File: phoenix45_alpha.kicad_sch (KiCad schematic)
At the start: 140 parts, among them J1 AVR-ISP-6, SW1 SW_PUSH, SW2 SW_PUSH, SW3 RotaryEncoder_Switch, U1 SRV05-4, U2 ATmega32U4-M, U3 ATmega32U4-M, X1 Crystal_GND24_Small

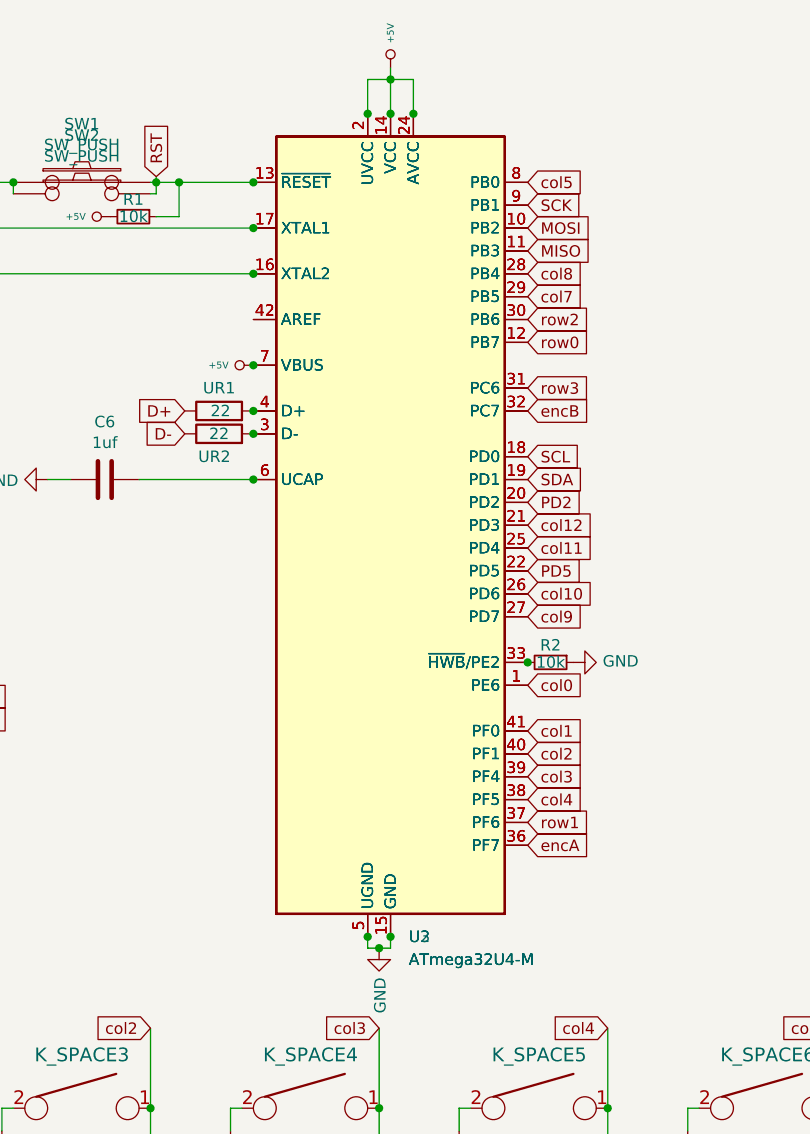
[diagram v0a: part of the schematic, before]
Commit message: atmega32u4-MU only
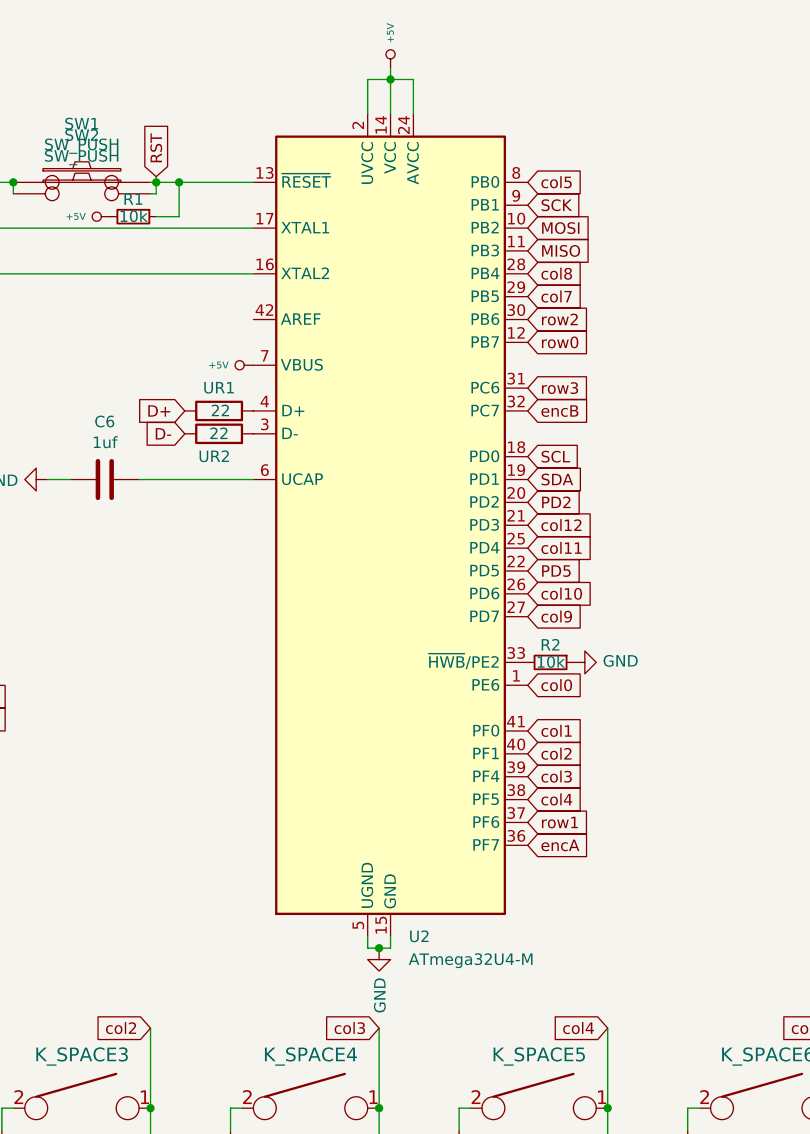
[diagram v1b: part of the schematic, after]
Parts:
- removed U3: ATmega32U4-M, Package_QFP:TQFP-44_10x10mm_P0.8mm, symbol MCU_Microchip_ATmega:ATmega32U4-M
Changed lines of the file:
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@@
   (junction (at 149.86 245.11) (diameter 0) (color 0 0 0 0)
   )
-  (junction (at 127 60.96) (diameter 0) (color 0 0 0 0)
-  )
   (junction (at 166.37 184.15) (diameter 0) (color 0 0 0 0)
   )
   (junction (at 233.045 66.675) (diameter 0) (color 0 0 0 0)
   )
-  (junction (at 142.24 48.26) (diameter 0) (color 0 0 0 0)
-  )
   (junction (at 140.97 158.75) (diameter 0) (color 0 0 0 0)
   )
@@
   (junction (at 140.97 140.97) (diameter 0) (color 0 0 0 0)
   )
-  (junction (at 139.7 139.7) (diameter 0) (color 0 0 0 0)
-  )
   (junction (at 251.46 219.71) (diameter 0) (color 0 0 0 0)
   )
   (junction (at 294.64 109.22) (diameter 0) (color 0 0 0 0)
   )
-  (junction (at 127 66.04) (diameter 0) (color 0 0 0 0)
-  )
   (junction (at 175.26 194.31) (diameter 0) (color 0 0 0 0)
   )
@@
   (junction (at 38.735 105.41) (diameter 0) (color 0 0 0 0)
   )
-  (junction (at 127 88.9) (diameter 0) (color 0 0 0 0)
-  )
   (junction (at 31.115 105.41) (diameter 0) (color 0 0 0 0)
   )
@@
   (junction (at 302.26 219.71) (diameter 0) (color 0 0 0 0)
   )
-  (junction (at 127 55.88) (diameter 0) (color 0 0 0 0)
-  )
   (junction (at 48.26 194.31) (diameter 0) (color 0 0 0 0)
   )
@@
   (junction (at 99.06 231.14) (diameter 0) (color 0 0 0 0)
   )
-  (junction (at 127 76.2) (diameter 0) (color 0 0 0 0)
-  )
   (junction (at 318.77 209.55) (diameter 0) (color 0 0 0 0)
   )
@@
   (junction (at 73.66 194.31) (diameter 0) (color 0 0 0 0)
   )
-  (junction (at 142.24 139.7) (diameter 0) (color 0 0 0 0)
-  )
   (junction (at 251.46 194.31) (diameter 0) (color 0 0 0 0)
   )
   (junction (at 318.77 158.75) (diameter 0) (color 0 0 0 0)
   )
-  (junction (at 139.7 48.26) (diameter 0) (color 0 0 0 0)
-  )
-  (junction (at 127 83.82) (diameter 0) (color 0 0 0 0)
-  )
   (junction (at 293.37 158.75) (diameter 0) (color 0 0 0 0)
   )
@@
   (junction (at 115.57 184.15) (diameter 0) (color 0 0 0 0)
   )
-  (junction (at 144.78 48.26) (diameter 0) (color 0 0 0 0)
-  )
   (junction (at 293.37 229.87) (diameter 0) (color 0 0 0 0)
   )
@@
   (junction (at 267.97 158.75) (diameter 0) (color 0 0 0 0)
   )
-  (junction (at 127 81.28) (diameter 0) (color 0 0 0 0)
-  )
   (junction (at 72.39 77.47) (diameter 0) (color 0 0 0 0)
   )
@@
   (junction (at 344.17 158.75) (diameter 0) (color 0 0 0 0)
   )
-  (junction (at 157.48 109.22) (diameter 0) (color 0 0 0 0)
-  )
   (junction (at 166.37 209.55) (diameter 0) (color 0 0 0 0)
   )
@@
     (pin "2")
   )
-  (symbol (lib_id "MCU_Microchip_ATmega:ATmega32U4-M") (at 142.24 93.98 0) (unit 1)
-    (in_bom yes) (on_board yes)
-    (property "Reference" "U3" (id 0) (at 144.2594 139.7 0)
-      (effects (font (size 1.27 1.27)) (justify left))
-    )
-    (property "Value" "ATmega32U4-M" (id 1) (at 144.2594 142.24 0)
-      (effects (font (size 1.27 1.27)) (justify left))
-    )
-    (property "Footprint" "Package_QFP:TQFP-44_10x10mm_P0.8mm" (id 2) (at 142.24 93.98 0)
-      (effects (font (size 1.27 1.27) italic) hide)
-    )
-    (property "Datasheet" "http://ww1.microchip.com/downloads/en/DeviceDoc/Atmel-7766-8-bit-AVR-ATmega16U4-32U4_Datasheet.pdf" (id 3) (at 142.24 93.98 0)
-      (effects (font (size 1.27 1.27)) hide)
-    )
-    (pin "1")
-    (pin "10")
-    (pin "11")
-    (pin "12")
-    (pin "13")
-    (pin "14")
-    (pin "15")
-    (pin "16")
-    (pin "17")
-    (pin "18")
-    (pin "19")
-    (pin "2")
-    (pin "20")
-    (pin "21")
-    (pin "22")
-    (pin "23")
-    (pin "24")
-    (pin "25")
-    (pin "26")
-    (pin "27")
-    (pin "28")
-    (pin "29")
-    (pin "3")
-    (pin "30")
-    (pin "31")
-    (pin "32")
-    (pin "33")
-    (pin "34")
-    (pin "35")
-    (pin "36")
-    (pin "37")
-    (pin "38")
-    (pin "39")
-    (pin "4")
-    (pin "40")
-    (pin "41")
-    (pin "42")
-    (pin "43")
-    (pin "44")
-    (pin "45")
-    (pin "5")
-    (pin "6")
-    (pin "7")
-    (pin "8")
-    (pin "9")
-  )
   (symbol (lib_id "keyboard_parts:KEYSW") (at 184.15 158.75 0) (unit 1)
     (in_bom yes) (on_board yes)
@@
       (reference "U2") (unit 1) (value "ATmega32U4-M") (footprint "Package_DFN_QFN:QFN-44-1EP_7x7mm_P0.5mm_EP5.2x5.2mm_ThermalVias")
     )
-    (path "/fe1a8f1c-b239-442d-acdc-13f4ebc5e42a"
-      (reference "U3") (unit 1) (value "ATmega32U4-M") (footprint "Package_QFP:TQFP-44_10x10mm_P0.8mm")
-    )
     (path "/5f7b6686-ca41-45e8-807e-4d2ae5a4c66e"
